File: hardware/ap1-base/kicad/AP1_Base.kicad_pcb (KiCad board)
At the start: 2 copper layers, 88 x 56 mm, 68 parts, among them J1 ENTRADA 12-24V, J3 +V SALIDA, J4 CANALES, J5 FOCOS CC, J6 AUX 12V, J7 PROGRAMADOR, Q1 BSC028N06LS3, Q2 BSC028N06LS3, Q3 BSC028N06LS3, Q4 BSC028N06LS3, Q5 AO3400A, U1 INA238, U2 LMR16006XDDC, U3 UCC27524D, U4 UCC27524D, U6 AL8860MP, U7 AL8860MP, U8 TMP1075D, U9 AT24CS02

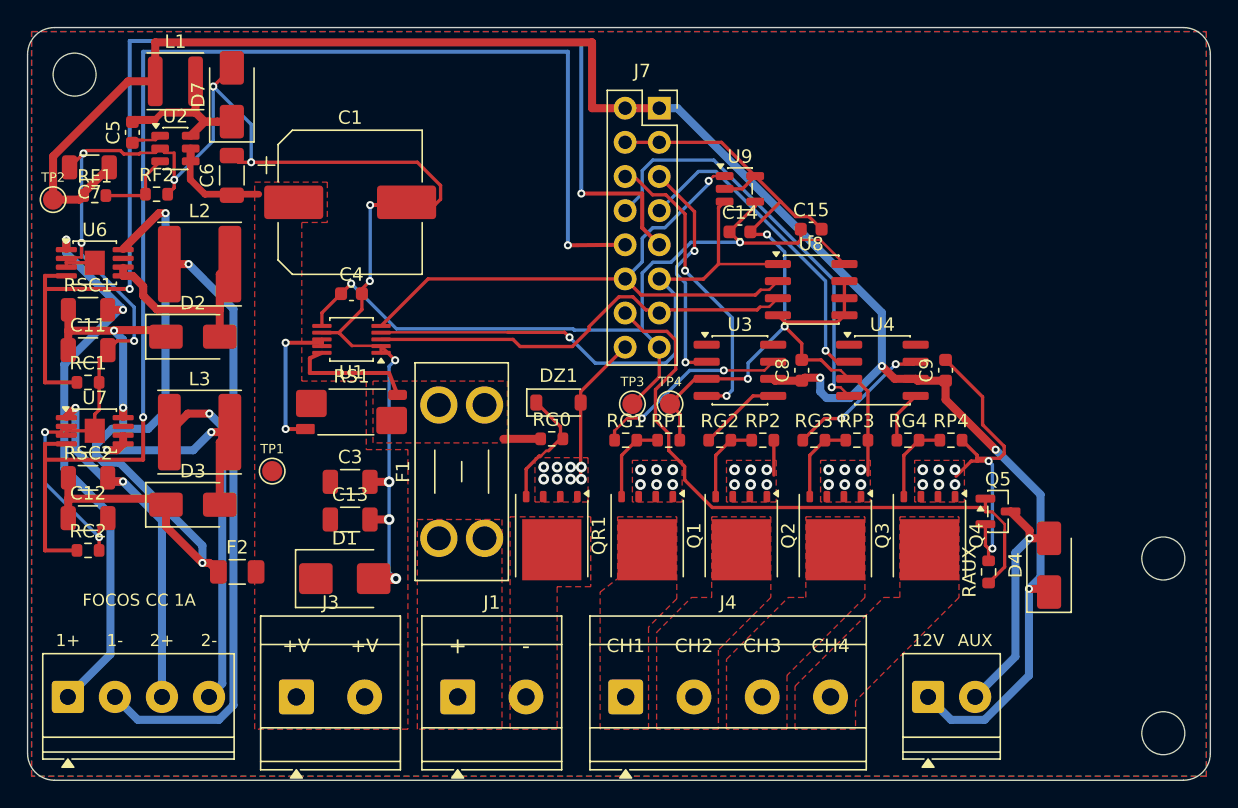
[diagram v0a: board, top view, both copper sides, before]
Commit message: AP-1 base a 4 capas, biblioteca JLCPCB y códigos LCSC automáticos
- placa.py: CAPAS=4 con planos internos (In1/In2 GND, tipo power para que
  Freerouting no rutee ahí), vías de costura GND (COSTURA) y zona sin cobre
  bajo la antena en todas las capas.
- AP1_Base: 4 capas JLC04161H-7628 (externas 2 oz, internas 1 oz), 61 vías de
  costura; ERC 0, DRC 0, 0 sin conectar, 0 diferencias.
- tools/jlcpcb.py + jlcpcb_catalogo.csv: 1499 piezas Basic/Preferred de la
  biblioteca JLCPCB-KiCad-Library (CDFER, MIT) y buscador por valor/huella.
- tools/descargar_biblioteca_jlcpcb.sh: instala la biblioteca para KiCad 9 y
  rehace el catálogo.
- salidas.py: BOM con LCSC y clase, RESUMEN_JLCPCB.txt con el cargo de piezas
  Extended, Gerber de todas las capas de cobre, PDF del lado inferior.
- Programador: D1/D2 SS14 -> B5819W (Preferred, misma huella).

Co-Authored-By: Claude Opus 5.5 <noreply@anthropic.com>
Claude-Session: https://claude.ai/code/session_01WVk3oGwfQfGTmAT2PMp8oW
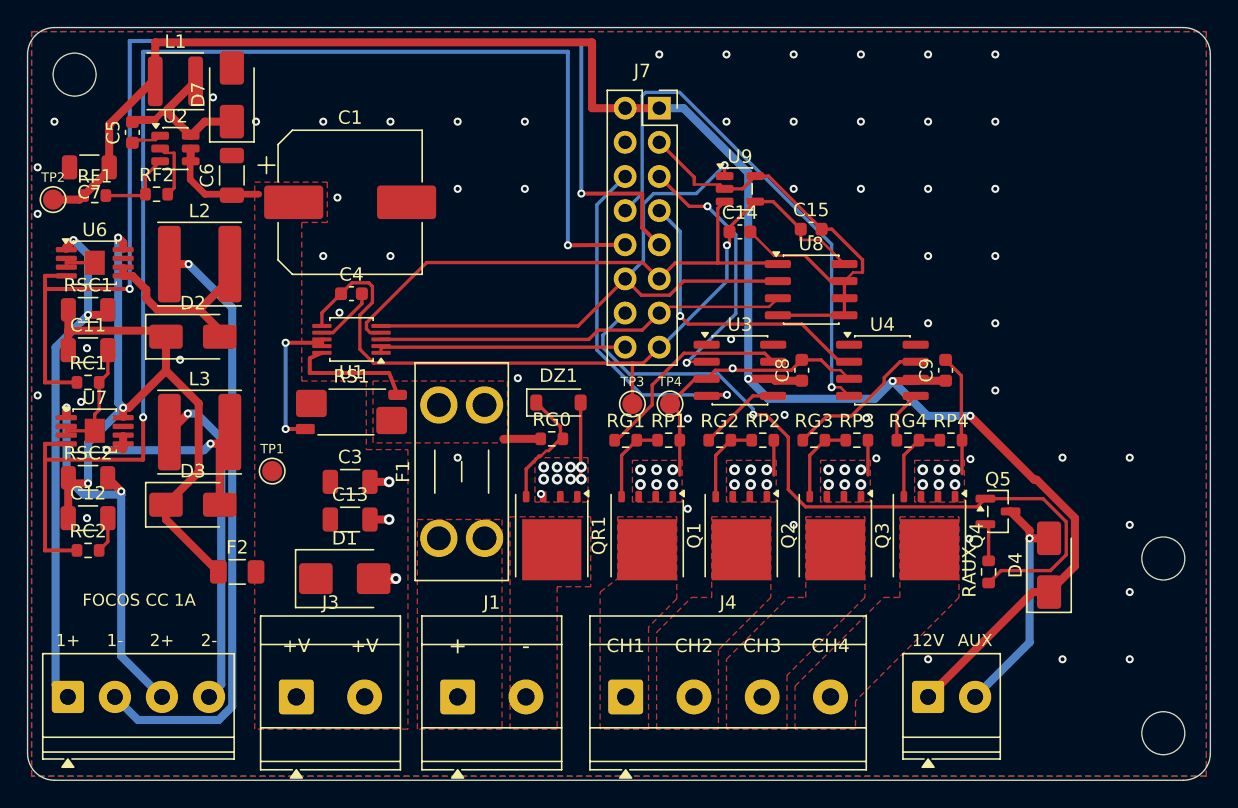
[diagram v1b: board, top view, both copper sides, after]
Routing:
- net /GND: track 248.4 -> 129.1 mm, vias 51 -> 95
- net /VCC: track 74.2 -> 61.9 mm, vias 4 -> 3
- net /PWM4: track 31.4 -> 40.2 mm
- net /AUX: track 47.4 -> 55.2 mm, vias 0 -> 1
- net /PWM2: track 22.3 -> 26.4 mm, vias 2 -> 1
- net /LEDA1: track 42.3 -> 38.4 mm
- net /V12: track 142.6 -> 138.8 mm, vias 4 -> 3
- net /SDA: track 43.3 -> 39.9 mm, vias 1 -> 0
- net /PWM1: track 17.4 -> 20.1 mm
- net /SCL: track 43.6 -> 46.1 mm
- net /PWM3: track 24.2 -> 22.5 mm
- net /LEDA2: track 27.1 -> 28.5 mm
- net /ALERT: track 32.4 -> 31.1 mm
- net /GO1: track 14.6 -> 15.6 mm, vias 2 -> 0
- net /SWC2: track 17.4 -> 16.7 mm
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- added copper zone on In1.Cu, net /GND
- added copper zone on In2.Cu, net /GND
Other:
- copper layers 2 -> 4

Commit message: AP-1: corte de MOSFET por hardware, supresor a la medida de los AL8860 y Home Assistant
- Base: la línea ALERTA (INA238 sobrecorriente/sobrevoltaje, TMP1075 85 C)
  apaga los dos UCC27524 por sus EN a través de D8/D9 (1N4148WS), sin
  depender del programa. Los diodos aíslan el pull-up interno de 12 V de los EN.
- Base: D1 SMBJ33A -> SMBJ26A. El anterior dejaba pasar hasta 53 V y los
  AL8860 aguantan 42 V; entrada máxima 26 V. Ruteada otra vez a 4 capas:
  ERC 0, DRC 0, 0 sin conectar, 0 diferencias.
- Programa fw 1.1: alerta del INA238 en menos de 1 ms (bus/temperatura a
  150 us), sobrevoltaje a 28 V, descubrimiento MQTT de Home Assistant (luz
  con brillo y efectos, AUX, focos CC, diagnóstico, sensores), varias órdenes
  por mensaje MQTT y 'O - b' para el foco 2 solo.

Co-Authored-By: Claude Opus 5.5 <noreply@anthropic.com>
Claude-Session: https://claude.ai/code/session_01WVk3oGwfQfGTmAT2PMp8oW
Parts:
- added D8: 1N4148WS, Diode_SMD:D_SOD-323, F.Cu at (151.6, 120.6)
- added D9: 1N4148WS, Diode_SMD:D_SOD-323, F.Cu at (165.4, 120.6)
- D1: value SMBJ33A -> SMBJ26A
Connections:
- U3 pad 1: unconnected-(U3-ENA-Pad1) -> /EN12
- U3 pad 8: unconnected-(U3-ENB-Pad8) -> /EN12
- U4 pad 1: unconnected-(U4-ENA-Pad1) -> /EN34
- U4 pad 8: unconnected-(U4-ENB-Pad8) -> /EN34
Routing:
- net /ALERT: track 31.1 -> 40.9 mm
- net /PWM4: track 40.2 -> 30.3 mm
- net /LEDK1: track 45.5 -> 35.9 mm
- net /EN34: track 0.00 -> 8.10 mm
- net /EN12: track 0.00 -> 7.79 mm
- net /SWC2: track 16.7 -> 24.1 mm
- net /PWM1: track 20.1 -> 25.2 mm, vias 2 -> 1
- net /SWC1: track 14.7 -> 18.4 mm
- net /3V3: track 60.0 -> 63.3 mm
- net /LEDK2: track 24.8 -> 21.7 mm
- net /GND: track 129.1 -> 132.0 mm, vias 95 -> 101
- net /VCC: track 61.9 -> 64.6 mm
- net /PWM3: track 22.5 -> 24.6 mm
- net /LEDA2: track 28.5 -> 27.5 mm, vias 2 -> 3
- net /V12: track 138.8 -> 139.6 mm, vias 3 -> 2
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
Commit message: Pedido más económico en JLCPCB: menos piezas Extended y BOM solo SMD
- Base: memoria AT24CS02 -> M24C02 (Preferred). El programa crea el número
  de serie (128 bits al azar con la MAC del programador) si la memoria no trae.
- Programador y AP-0.2: botones TL3342 -> TS-1187A (Basic, misma huella).
  En la AP-0.2 se cambió la huella sin volver a rutear: DRC 0.
- Base: rutas fijas para SWC1/SWC2 y CC2 igual que CC1 (el canal 2 es
  copia del 1, 12.5 mm abajo). Ruteo estable: ERC 0, DRC 0, 0 sin conectar.
- salidas.py: BOM/CPL '_solo_SMD' para soldar a mano clemas y conectores,
  resumen con cargo por código LCSC distinto y costo de piezas Basic.
- jlcpcb.py: piezas reconocidas por huella (botones con valor de etiqueta).
- Cargo de montaje por pedido: base+programador de ~93 a ~84 USD, o ~54 USD
  en el pedido solo SMD.

Co-Authored-By: Claude Opus 5.5 <noreply@anthropic.com>
Claude-Session: https://claude.ai/code/session_01WVk3oGwfQfGTmAT2PMp8oW
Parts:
- U9: value AT24CS02 -> M24C02-WMN6TP; footprint Package_TO_SOT_SMD:SOT-23-5 -> Package_SO:SOIC-8_3.9x4.9mm_P1.27mm
- moved U9 2.50 mm to (153.0, 109.5)
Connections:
- U9 pad 1: /SCL -> /GND
- U9 pad 3: /SDA -> /GND
- U9 pad 4: /3V3 -> /GND
- U9 pad 5: /GND -> /SDA
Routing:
- net /GND: track 132.0 -> 101.9 mm, vias 101 -> 93
- net /3V3: track 63.3 -> 80.7 mm
- net /VCC: track 64.6 -> 71.5 mm
- net /PWM3: track 24.6 -> 18.8 mm
- net /PWM2: track 26.8 -> 21.4 mm
- net /SWC2: track 24.1 -> 19.0 mm, vias 2 -> 0
- net /SCL: track 45.8 -> 42.7 mm, vias 1 -> 0
- net /V12: track 139.6 -> 142.6 mm
- net /LEDA2: track 27.5 -> 25.9 mm
- net /PWM4: track 30.3 -> 31.5 mm
- net /SDA: track 40.3 -> 41.2 mm
- net /GO3: track 11.1 -> 12.0 mm
- net /CC2: track 99.8 -> 99.0 mm
- net /AUX: track 55.9 -> 55.2 mm

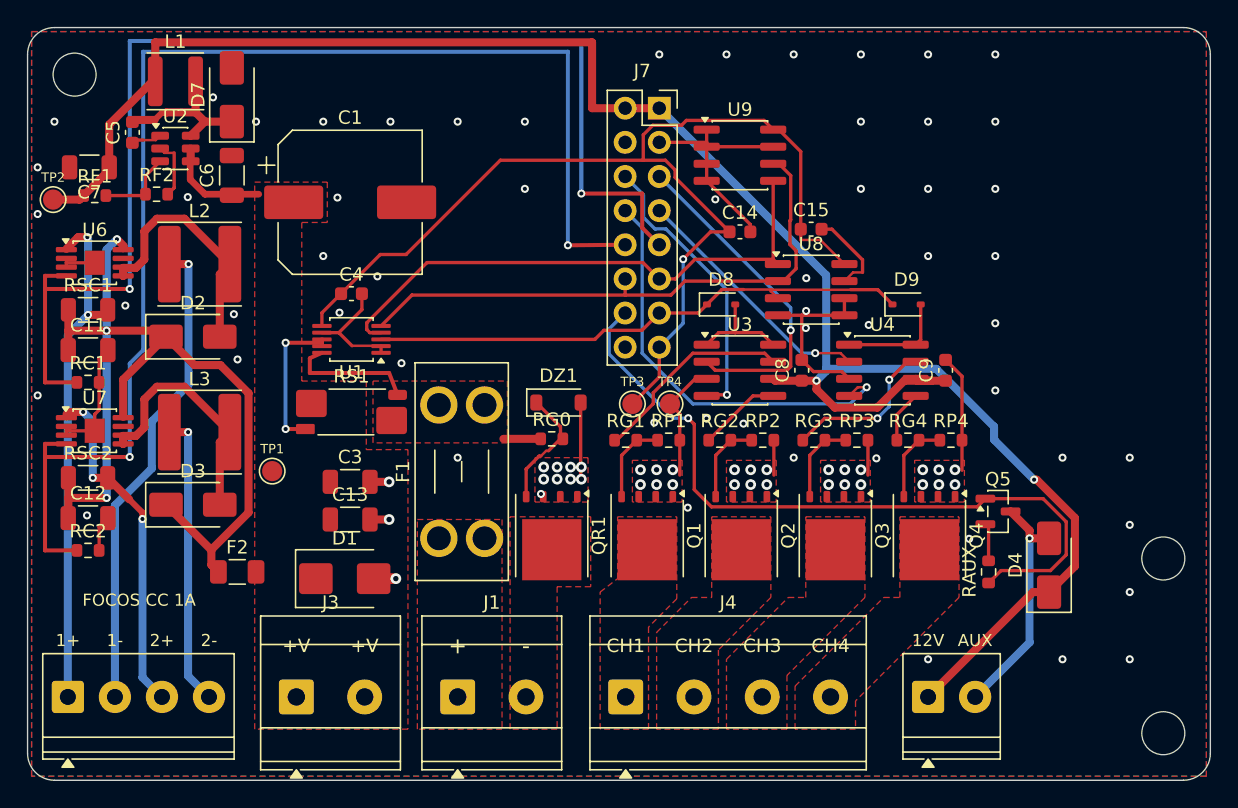
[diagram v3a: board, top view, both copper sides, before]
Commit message: Listo para JLCPCB: códigos LCSC, reglas de fabricación y carpeta de pedido
- Códigos LCSC verificados para todas las piezas SMD (INA238, LMR16006,
  UCC27524, AL8860, TMP1075, MOSFET, bobinas, capacitor, fusible, módulo,
  conectores) en tools/jlcpcb.py; piezas reconocidas por huella.
- Shunt: el WSK2512 de 4 terminales se agotó en LCSC; base y AP-0.2 usan un
  HoJLR2512 1 mOhm 2 W (C2924520) con huella propia 'net tie' que conserva
  el sensado Kelvin (tools/huellas/LetreroLab.pretty).
- ESP32-C3-WROOM-02: huella propia con 4 vías de 0.3 mm en lugar de 12 de
  0.2 mm (proceso estándar de JLCPCB). Textos de serigrafía de 0.8 mm o más.
- IND: fusible de 3 A (el mismo de la base).
- AP-0.2 ruteada otra vez con el nuevo shunt.
- Las 4 placas: ERC 0, DRC 0, 0 sin conectar, 0 diferencias y 0 problemas
  con las reglas de fabricación de JLCPCB.
- PEDIDO_JLCPCB/ (+ .zip) con Gerber, BOM y CPL completos o solo SMD por
  placa, y PEDIDO_JLCPCB.md con las opciones exactas del pedido.

Co-Authored-By: Claude Opus 5.5 <noreply@anthropic.com>
Claude-Session: https://claude.ai/code/session_01WVk3oGwfQfGTmAT2PMp8oW
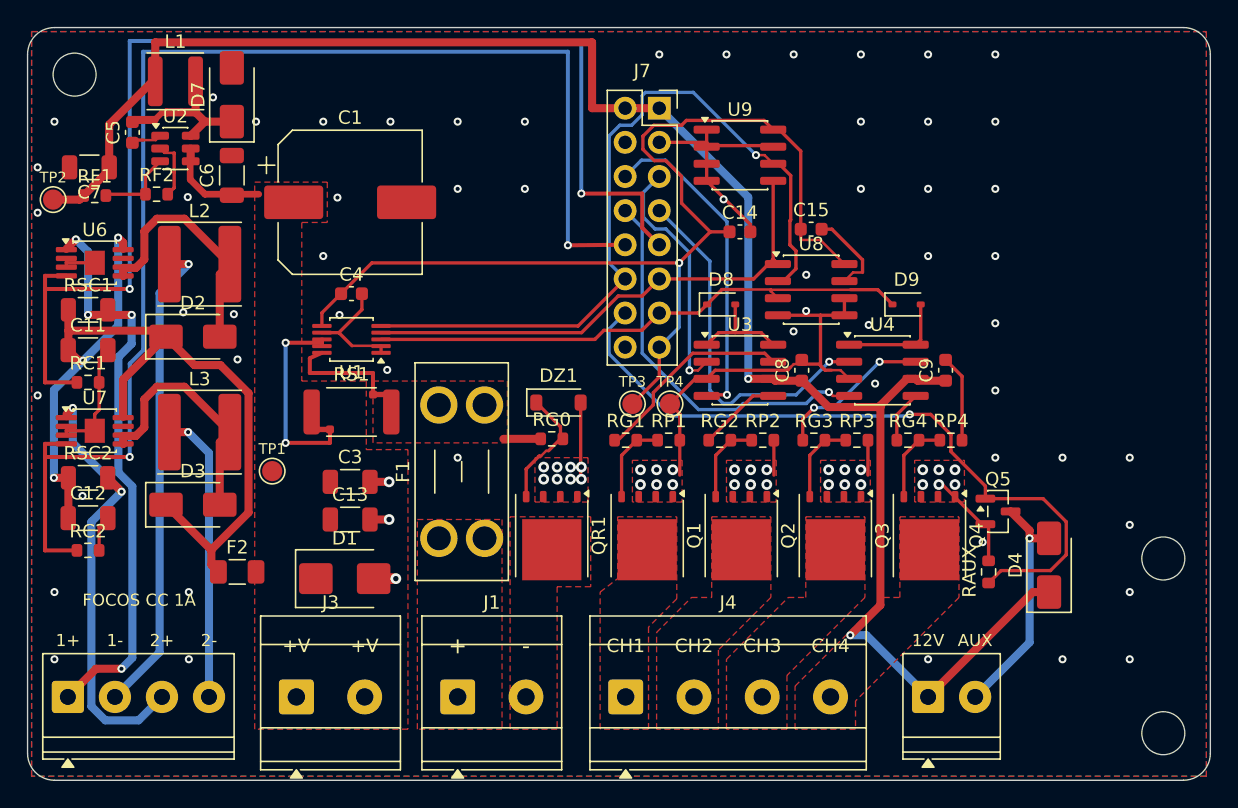
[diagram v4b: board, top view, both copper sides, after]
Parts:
- RS1: value 1mR 2512 Kelvin -> 1mR 2512 2W; footprint Resistor_SMD:R_Shunt_Vishay_WSK2512_6332Metric_T1.19mm -> LetreroLab:R_2512_Kelvin_NetTie
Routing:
- net /SCL: track 42.7 -> 57.8 mm, vias 0 -> 1
- net /GND: track 101.9 -> 112.1 mm, vias 93 -> 92
- net /PWM3: track 18.8 -> 27.0 mm
- net /LEDA2: track 25.9 -> 33.4 mm, vias 3 -> 2
- net /V12: track 142.6 -> 135.8 mm
- net /PWM1: track 24.8 -> 18.4 mm
- net /LEDA1: track 38.4 -> 42.9 mm, vias 2 -> 4
- net /ISN: track 11.1 -> 15.0 mm
- net /PWM2: track 21.4 -> 24.4 mm
- net /SDA: track 41.2 -> 38.3 mm
- net /PWM4: track 31.5 -> 28.9 mm
- net /AUX: track 55.2 -> 53.2 mm
- net /3V3: track 80.7 -> 79.2 mm
- net /ISP: track 9.73 -> 8.38 mm
- net /SWC2: track 19.0 -> 18.4 mm

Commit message: AP CONNECT: sin borneras en todas las placas, placa nueva AP PRO AI4 y guía de fabricantes
- Borneras de tornillo reemplazadas por conectores con cable y código LCSC verificado:
  XT60 (C98732), JST VH 2/3/4 (C160315/6/7), JST XH 2/3/4 (C158012, C144394/5), Qwiic
  en BASE, IND, PIX, DMX, PLANTILLA, AP INPUT, AP OUTPUT y DIST 4; zonas de potencia rehechas
- XT60 de la DIST 4 con la polaridad marcada en la huella (pata 1 = -, pata 2 = +)
- TCA9554PWR ya con código (C477924)
- ap1-ai4: 4 entradas 0-10 V / 4-20 mA con ADS1115 (C37593), +24 V para sensores de lazo
- Programa 1.7: lectura AI4, umbrales con acciones, Home Assistant, tarjeta en la app
- FABRICANTES.md: JLCPCB, PCBWay, Seeed, NextPCB, México; impresión 3D y tornillería
- Pedido JLCPCB con 10 placas (AP-0.2 retirada); ERC/DRC/DFM 0 en todas

Co-Authored-By: Claude Opus 5.5 <noreply@anthropic.com>
Claude-Session: https://claude.ai/code/session_01WVk3oGwfQfGTmAT2PMp8oW
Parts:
- added J8: FOCO CC 2, Connector_JST:JST_XH_B2B-XH-A_1x02_P2.50mm_Vertical, F.Cu at (111.6, 151.0)
- J1: footprint TerminalBlock_Phoenix:TerminalBlock_Phoenix_MKDS-3-2-5.08_1x02_P5.08mm_Horizontal -> Connector_JST:JST_VH_B4P-VH_1x04_P3.96mm_Vertical
- J3: footprint TerminalBlock_Phoenix:TerminalBlock_Phoenix_MKDS-3-2-5.08_1x02_P5.08mm_Horizontal -> Connector_JST:JST_VH_B2P-VH_1x02_P3.96mm_Vertical
- J4: footprint TerminalBlock_Phoenix:TerminalBlock_Phoenix_MKDS-3-4-5.08_1x04_P5.08mm_Horizontal -> Connector_JST:JST_VH_B4P-VH_1x04_P3.96mm_Vertical
- J5: value FOCOS CC -> FOCO CC 1; footprint TerminalBlock_Phoenix:TerminalBlock_Phoenix_PT-1,5-4-3.5-H_1x04_P3.50mm_Horizontal -> Connector_JST:JST_XH_B2B-XH-A_1x02_P2.50mm_Vertical
- J6: footprint TerminalBlock_Phoenix:TerminalBlock_Phoenix_PT-1,5-2-3.5-H_1x02_P3.50mm_Horizontal -> Connector_JST:JST_XH_B2B-XH-A_1x02_P2.50mm_Vertical
- moved J4 3.55 mm to (148.0, 150.4)
- moved J1 2.09 mm to (130.0, 150.4)
- moved J6 1.30 mm to (166.5, 151.0)
- moved J5 1.20 mm to (103.0, 151.0)
- moved J3 0.72 mm to (119.6, 150.4)
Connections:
- J1 pad 2: /GNDIN -> /VIN_RAW
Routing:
- net /GND: track 112.1 -> 96.3 mm, vias 92 -> 99
- net /SCL: track 57.8 -> 45.6 mm, vias 1 -> 0
- net /SDA: track 38.3 -> 46.4 mm, vias 0 -> 1
- net /AUX: track 53.2 -> 46.3 mm
- net /VCC: track 71.5 -> 65.9 mm, vias 3 -> 4
- net /3V3: track 79.2 -> 84.5 mm, vias 1 -> 2
- net /PWM4: track 28.9 -> 25.1 mm
- net /PWM3: track 27.0 -> 23.1 mm
- net /PWM1: track 18.4 -> 22.0 mm
- net /LEDA1: track 42.9 -> 39.8 mm, vias 4 -> 2
- net /AUXD: track 17.5 -> 20.1 mm
- net /LEDK1: track 35.9 -> 38.4 mm
- net /GO1: track 15.3 -> 17.3 mm
- net /LEDA2: track 33.4 -> 31.8 mm, vias 2 -> 3
- net /LEDK2: track 21.7 -> 23.2 mm
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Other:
- board text added: "+ + - -"
- board text added: "+V +V"
- board text added: "1 2 3 4"
- board text added: "CC1"
- board text added: "CC2"
- board text removed: "+"
- board text removed: "+V"
- board text removed: "-"
- board text removed: "1+"
- board text removed: "1-"
- board text removed: "12V"
- board text removed: "2+"
- board text removed: "2-"
- board text removed: "CH1"
- board text removed: "CH2"
- board text removed: "CH3"
- board text removed: "CH4"
- board text removed: "FOCOS CC 1A"
